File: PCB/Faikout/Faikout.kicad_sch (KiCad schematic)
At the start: 47 parts, among them J1 1x5, J2 TC2030-USB-NL, J3 Reset, Q1 BSS138PS, U1 TPS562246, U4 ESP32-S3-MINI-1

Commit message: Started on POE
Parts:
- J1: value 1x5 -> S21
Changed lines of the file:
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@@
 			)
 		)
-		(property "Value" "1x5"
+		(property "Value" "S21"
 			(at 201.295 88.3721 0)
 			(show_name no)

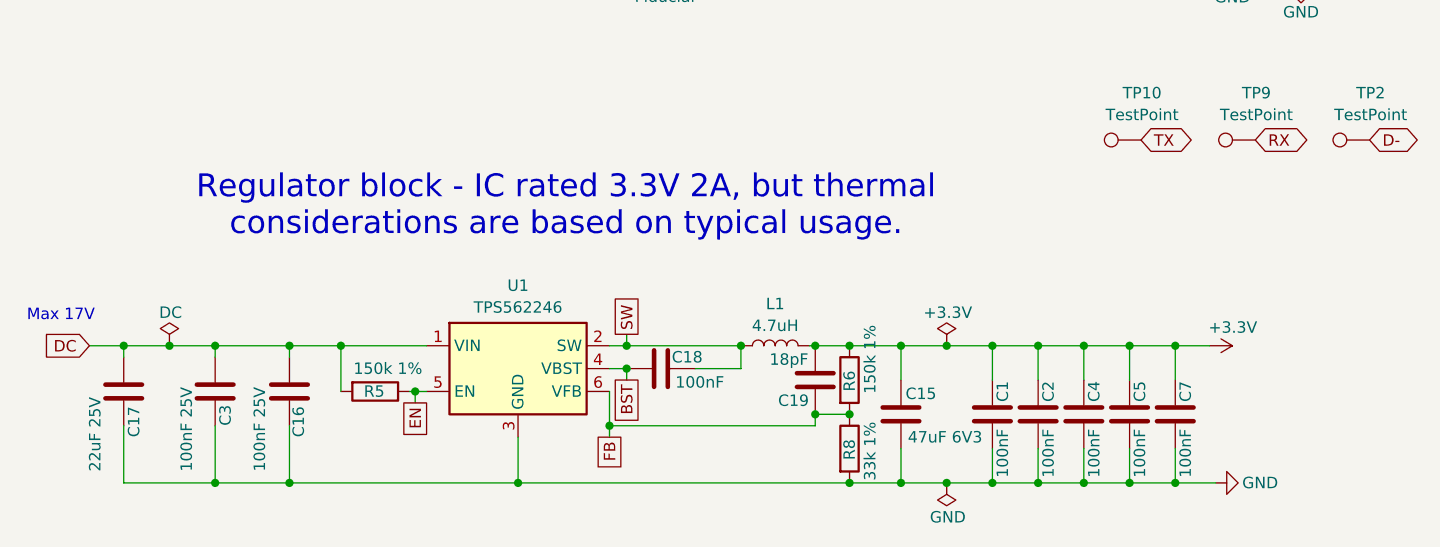
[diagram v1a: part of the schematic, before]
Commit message: New regulator
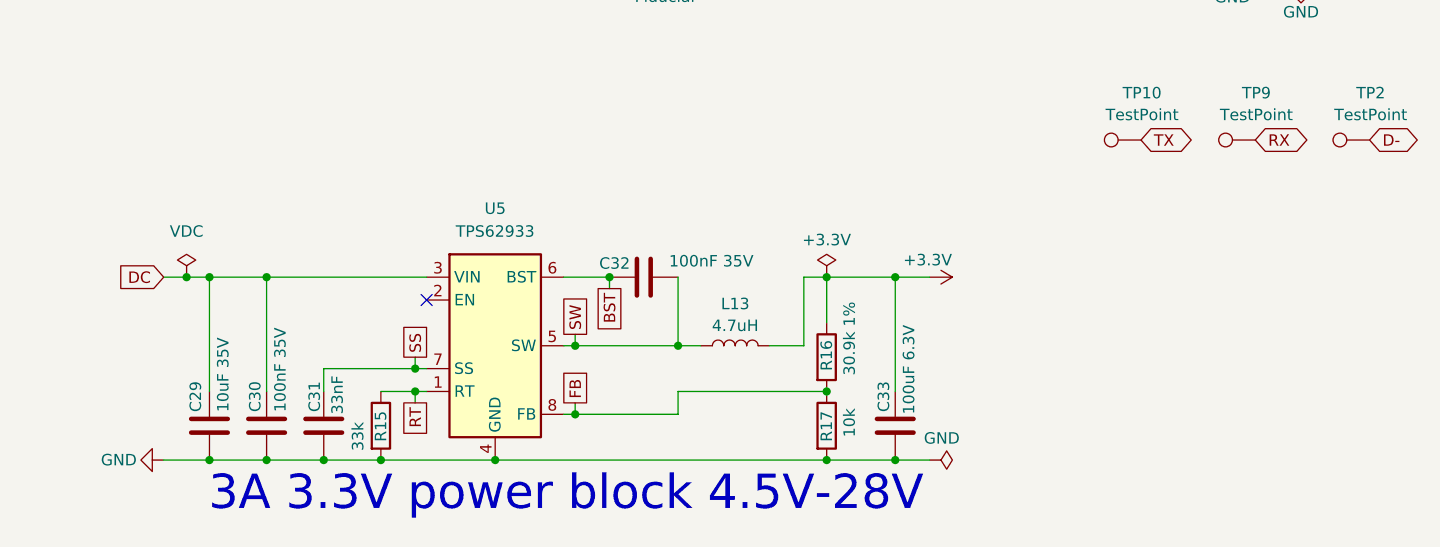
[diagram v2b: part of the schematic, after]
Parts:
- removed C1, C18, C2, C4, C5, C7: 100nF, RevK:C_0201, symbol Device:C
- removed C15: 47uF 6V3, RevK:C_0805, symbol Device:C
- removed C16, C3: 100nF 25V, RevK:C_0402, symbol Device:C
- removed C17: 22uF 25V, RevK:C_0805, symbol Device:C
- removed C19: 18pF, RevK:C_0201, symbol Device:C
- removed L1: 4.7uH, RevK:L_5x5, symbol Device:L
- removed R5, R6: 150k 1%, RevK:R_0201, symbol Device:R
- removed R8: 33k 1%, RevK:R_0201, symbol Device:R
- removed U1: TPS562246, RevK:SOT-5x3-6, symbol RevK:TPS562246
- added C29: 10uF 35V, RevK:C_0603, symbol Device:C
- added C30, C32: 100nF 35V, RevK:C_0201, symbol Device:C
- added C31: 33nF, RevK:C_0201, symbol Device:C
- added C33: 100uF 6.3V, RevK:C_0805, symbol Device:C
- added L13: 4.7uH, RevK:L_5x5, symbol Device:L
- added R15: 33k, RevK:R_0201, symbol Device:R
- added R16: 30.9k 1%, RevK:R_0201, symbol Device:R
- added R17: 10k, RevK:R_0201, symbol Device:R
- added U5: TPS62933, RevK:SOT-583-8, symbol Regulator_Switching:TPS62933
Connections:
- net +3.3V: now also C33.1, L13.2, R16.1
- net BST: now also C32.1, U5.6 (BST)
- net DC: now also C29.1, C30.1, U5.3 (VIN)
- net FB: now also R16.2, R17.1, U5.8 (FB)
- net GND: now also C29.2, C30.2, C31.2, C33.2, R15.2, R17.2, U5.4 (GND)
- net SW: now also C32.2, L13.1, U5.5 (SW)
- new net RT: R15.1, U5.1 (RT)
- new net SS: C31.1, U5.7 (SS)
- no-connect marks 24 -> 25
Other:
- note added: "3A 3.3V power block 4.5V-28V"
- note removed: "Regulator block - IC rated 3.3V 2A, but thermal considerations are based on typical usage."
